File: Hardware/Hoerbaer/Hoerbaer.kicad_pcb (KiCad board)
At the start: 4 copper layers, 80 x 88 mm, 198 parts, among them J1 I2C, J12 Battery 1S Li-Ion, J13 JTAG, J14 Speaker_L, J15 Speaker_R, J16 USB2_UART, J17 RST_BOOT, J2 DISPLAY, J3 Micro_SD_Card_Det1, J4 USB1, J5 ENCODER, J6 PAW_A, J7 PAW_B, J8 PAW_C, J9 PAW_D, Q1 DMG3415UQ-7, Q5 S8050, Q6 S8050, SW1 RESET, SW2 PROG, U1 ESP32 S3 MINI, U10 TAS5805M, U11 CH343P, U12 MAX17048G, U13 TPS61288, U2 PCF8574APWR, U3 PCF8574APWR, U4 PCF8574APWR, U5 TLC59108xPW, U6 TLC59108xPW, U7 TLC59108xPW, U8 MCP73831T-2ACI/OT (4.2V), U9 TPS63001

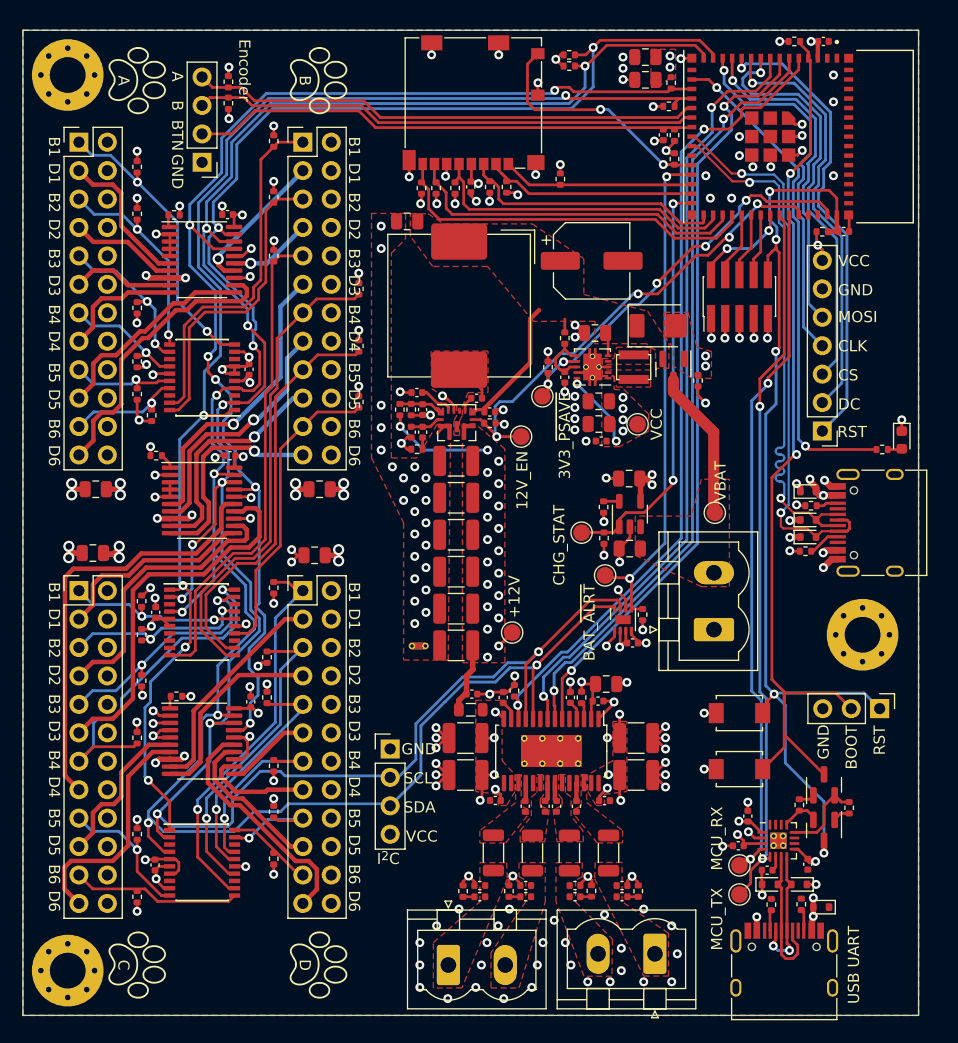
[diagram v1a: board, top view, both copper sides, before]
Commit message: Fixed net tie ground plane issue.
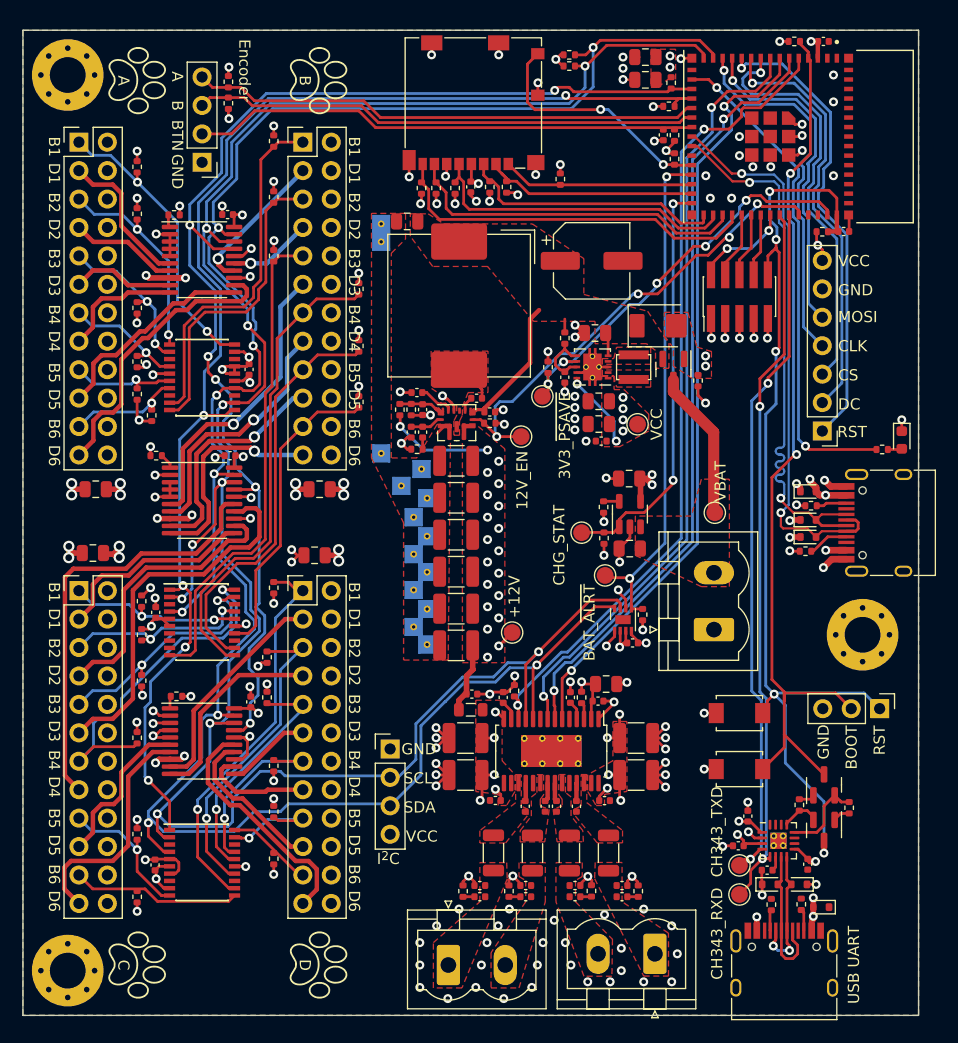
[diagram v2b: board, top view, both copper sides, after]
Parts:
- removed REF**: OSHW-Logo_11.4x12mm_SilkScreen, Symbol:OSHW-Logo_11.4x12mm_SilkScreen
- added NT10: GNDs, Baer_Footprints:NetTie-2_Via, F.Cu at (94.9, 110.0)
- added NT11: GNDs, Baer_Footprints:NetTie-2_Via, F.Cu at (94.9, 113.3)
- added NT12: GNDs, Baer_Footprints:NetTie-2_Via, F.Cu at (92.0, 77.3)
- added NT13: GNDs, Baer_Footprints:NetTie-2_Via, F.Cu at (92.0, 97.8)
- added NT14: GNDs, Baer_Footprints:NetTie-2_Via, F.Cu at (93.8, 100.7)
- added NT2: GNDs, Baer_Footprints:NetTie-2_Via, F.Cu at (96.1, 111.7)
- added NT3: GNDs, Baer_Footprints:NetTie-2_Via, F.Cu at (96.1, 101.8)
- added NT4: GNDs, Baer_Footprints:NetTie-2_Via, F.Cu at (96.1, 105.2)
- added NT5: GNDs, Baer_Footprints:NetTie-2_Via, F.Cu at (96.1, 108.4)
- added NT6: GNDs, Baer_Footprints:NetTie-2_Via, F.Cu at (96.1, 114.9)
- added NT7: GNDs, Baer_Footprints:NetTie-2_Via, F.Cu at (95.6, 99.2)
- added NT8: GNDs, Baer_Footprints:NetTie-2_Via, F.Cu at (94.9, 103.5)
- added NT9: GNDs, Baer_Footprints:NetTie-2_Via, F.Cu at (94.9, 106.8)
- NT1: footprint NetTie:NetTie-2_THT_Pad0.3mm -> Baer_Footprints:NetTie-2_Via
- R53: value 190kΩ -> 191kΩ
- TP2: value MCU_TX -> CH343_RXD
- TP3: value MCU_RX -> CH343_TXD
- moved NT1 36.2 mm to (92.0, 78.9), turned to 180 degrees
- moved J4 0.77 mm to (137.6, 104.0)
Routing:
- net GND: track 166.4 -> 167.9 mm, vias 175 -> 152
- net /USB1_D+: track 48.7 -> 50.3 mm
- net VBUS: track 45.6 -> 46.6 mm
- net Net-(J4-CC2): track 1.97 -> 2.74 mm
- net Net-(J4-CC1): track 2.91 -> 3.68 mm
- net /USB1_D-: track 49.5 -> 50.3 mm
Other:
- board text added: "TODO: Zonen rund um GNDPWR"

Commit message: Many small corrections, changed connectors, ...
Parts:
- added J10: Battery 1S Li-Ion, Connector_Wire:SolderWire-0.5sqmm_1x02_P4.6mm_D0.9mm_OD2.1mm, F.Cu at (124.2, 114.8)
- J12: footprint Connector_Phoenix_MSTB:PhoenixContact_MSTBVA_2,5_2-G-5,08_1x02_P5.08mm_Vertical -> Connector_JST:JST_XH_B2B-XH-AM_1x02_P2.50mm_Vertical
- J14, J15: footprint Connector_Phoenix_MSTB:PhoenixContact_MSTBVA_2,5_2-G-5,08_1x02_P5.08mm_Vertical -> TerminalBlock:TerminalBlock_bornier-2_P5.08mm
- moved J14 5.65 mm to (111.0, 144.0), turned to 0 degrees
- moved TP5 3.96 mm to (121.1, 107.0)
- moved J12 3.26 mm to (118.5, 113.8)
- moved C48 0.61 mm to (100.2, 136.4)
- moved C53 0.61 mm to (100.2, 137.4)
- moved R65 0.61 mm to (98.7, 136.9)
- moved R63 0.59 mm to (115.5, 136.9)
- moved C46 0.59 mm to (114.1, 136.4)
- moved C51 0.59 mm to (114.1, 137.4)
- moved FB4 0.53 mm to (101.5, 133.5)
- moved J15 0.50 mm to (98.0, 144.0)
- moved FB2 0.39 mm to (112.7, 133.5)
- moved C24 0.36 mm to (86.2, 101.1)
- moved C22 0.20 mm to (66.3, 101.0)
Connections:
- J14 pad 1: /Audio/SPEAKER_A+ -> /Audio/SPEAKER_A-
- J14 pad 2: /Audio/SPEAKER_A- -> /Audio/SPEAKER_A+
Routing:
- net GND: vias 152 -> 161
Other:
- board text added: "+"
- board text added: "-"
- board text added: "L"
- board text added: "R"
- board text removed: "TODO: Zonen rund um GNDPWR"
